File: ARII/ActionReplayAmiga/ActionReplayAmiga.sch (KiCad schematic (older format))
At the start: 33 parts, among them J0 A2000_CPUSLOT_EDGE_LOGICAL, Q0 MOSFET_PCH-DMG2307L, SW0 SW_SPST, SW1 SW_SPDT, U0 TIF044 FS F74, U1 16L8-25C (TI036FF), U10 27C512-15_PLCC, U2 16L8-25C (TI036FF), U3 16L8-25C (TI036FF), U4 16L8-25C (TI042FF)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

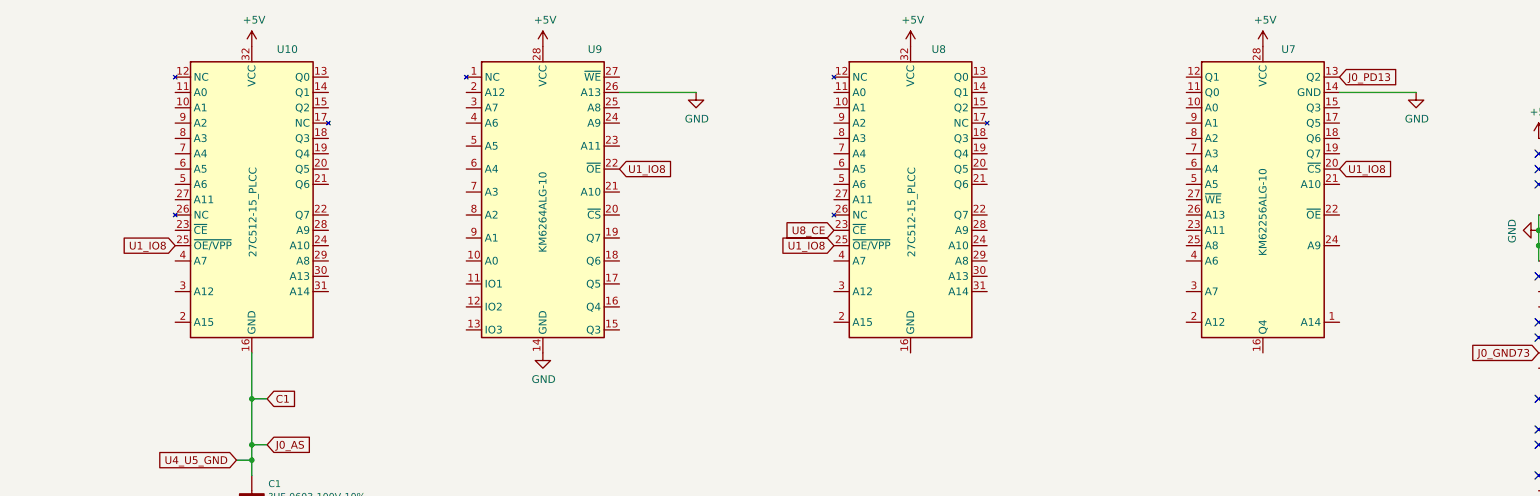
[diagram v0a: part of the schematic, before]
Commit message: Fixed Layouts of KM62256ALG and 27C512-15
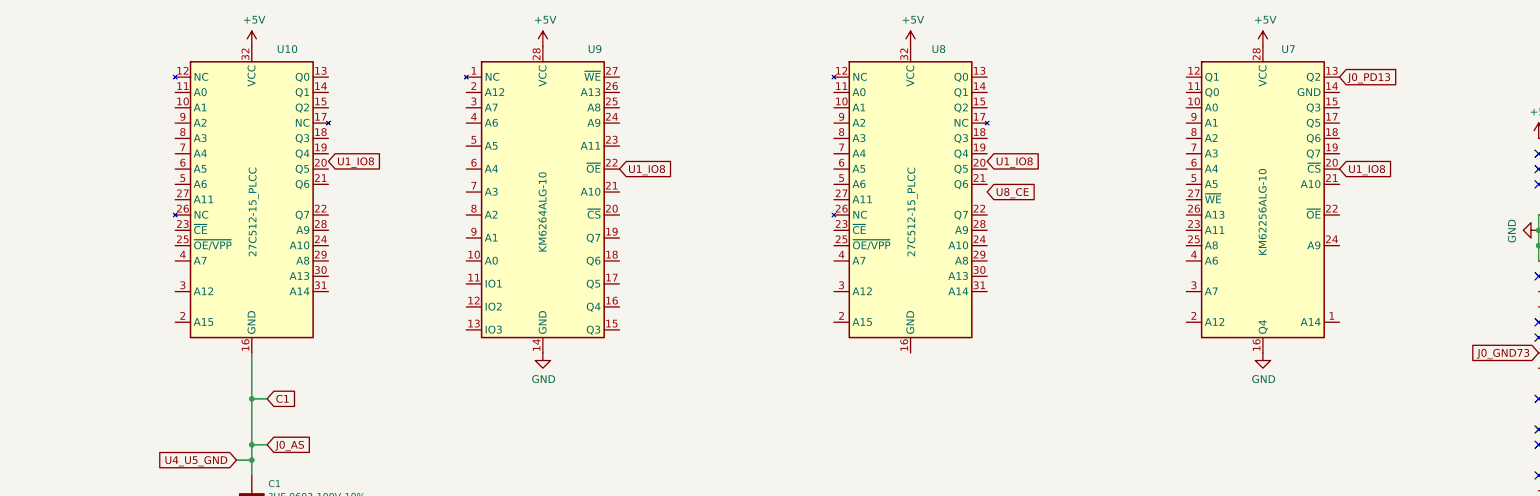
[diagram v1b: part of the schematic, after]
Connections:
- net GND: now also U7.16 (Q4); no longer U7.14 (GND), U9.26 (A13)
- net U1_IO8: no longer U10.25 (~OE/VPP), U8.25 (~OE/VPP)
- net U8_CE: no longer U8.23 (~CE)
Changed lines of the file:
@@
 Wire Notes Line
 	7050 7400 7050 6650
-Text GLabel 4150 2350 0    50   Input ~ 0
+Text GLabel 5150 1800 2    50   Input ~ 0
 U1_IO8
 Text GLabel 3600 4950 2    50   Input ~ 0
@@
 $Comp
 L power:GND #PWR?
-U 1 1 5FF48F3E
-P 7550 1350
-F 0 "#PWR?" H 7550 1100 50  0001 C CNN
-F 1 "GND" H 7555 1177 50  0000 C CNN
-F 2 "" H 7550 1350 50  0001 C CNN
-F 3 "" H 7550 1350 50  0001 C CNN
-	1    7550 1350
-	1    0    0    -1
-$EndComp
-Wire Wire Line
-	7050 1350 7550 1350
-$Comp
-L power:GND #PWR?
 U 1 1 5FB2E5AA
 P 6550 3050
@@
 	1    0    0    -1
 $EndComp
-Text GLabel 8450 2350 0    50   Input ~ 0
+Text GLabel 9450 1800 2    50   Input ~ 0
 U1_IO8
 $Comp
@@
 	1    0    0    -1
 $EndComp
-Text GLabel 8450 2250 0    50   Input ~ 0
+Text GLabel 9450 2000 2    50   Input ~ 0
 U8_CE
 $Comp
@@
 L power:GND #PWR?
 U 1 1 5FB2FA5B
-P 12250 1350
-F 0 "#PWR?" H 12250 1100 50  0001 C CNN
-F 1 "GND" H 12255 1177 50  0000 C CNN
-F 2 "" H 12250 1350 50  0001 C CNN
-F 3 "" H 12250 1350 50  0001 C CNN
-	1    12250 1350
-	1    0    0    -1
-$EndComp
-Text GLabel 11750 1250 2    50   Input ~ 0
-J0_PD13
-Wire Wire Line
-	11750 1350 12250 1350
+P 11250 3050
+F 0 "#PWR?" H 11250 2800 50  0001 C CNN
+F 1 "GND" H 11255 2877 50  0000 C CNN
+F 2 "" H 11250 3050 50  0001 C CNN
+F 3 "" H 11250 3050 50  0001 C CNN
+	1    11250 3050
+	1    0    0    -1
+$EndComp
 $Comp
 L power:+5V #PWR?
@@
 	1    0    0    -1
 $EndComp
-Text GLabel 11750 1850 2    50   Input ~ 0
-U1_IO8
 $Comp
 L ActionReplayAmiga:KM6264ALG-10 U9
@@
 	1    0    0    -1
 $EndComp
+Text GLabel 11750 1850 2    50   Input ~ 0
+U1_IO8
+Text GLabel 11750 1250 2    50   Input ~ 0
+J0_PD13
 $EndSCHEMATC

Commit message: U2 Completed
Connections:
- net U2_I1: now reaches U2.1 (I1)
- net U2_I1: now also U3.1 (I1)
- net U9_CS1: now reaches U2.16 (IO4)
- net U9_CS1: now also U9.20 (~CS)
- net U9_IO1: now reaches U2.17 (I03)
- net U9_IO1: now also U9.11 (IO1)
- net U9_IO2: now reaches U2.18 (IO2)
- net U9_IO2: now also U9.12 (IO2)
- net U7_CS: now reaches U2.19 (IO1)
- net U7_CS: now also U7.22 (~OE)
- net U2_I2: now reaches U2.2 (I2)
- net U2_I2: now also U3.2 (I2)
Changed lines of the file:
@@
 Text GLabel 11750 1250 2    50   Input ~ 0
 J0_PD13
+Text GLabel 7050 2150 2    50   Input ~ 0
+U9_CS1
+Text GLabel 6200 4650 2    50   Input ~ 0
+U9_CS1
+Text GLabel 6050 2600 0    50   Input ~ 0
+U9_IO1
+Text GLabel 6200 4550 2    50   Input ~ 0
+U9_IO1
+Text GLabel 6050 2750 0    50   Input ~ 0
+U9_IO2
+Text GLabel 6200 4450 2    50   Input ~ 0
+U9_IO2
+Text GLabel 11750 2150 2    50   Input ~ 0
+U7_CS
+Text GLabel 6200 4350 2    50   Input ~ 0
+U7_CS
+Text GLabel 5200 4450 0    50   Input ~ 0
+U2_I2
+Text GLabel 6950 4400 0    50   Input ~ 0
+U2_I2
+Text GLabel 5200 4350 0    50   Input ~ 0
+U2_I1
+Text GLabel 6950 4300 0    50   Input ~ 0
+U2_I1
 $EndSCHEMATC

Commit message: U3 Completed
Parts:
- removed SW0: SW_SPST, symbol Switch:SW_SPST
- added S0: GPTS203211B, digikey-footprints:PushButton_12x12mm_THT_GPTS203211B, symbol dk_Pushbutton-Switches:GPTS203211B
- gave numbers to parts that had none: 1
- renumbered SW1 to SW0
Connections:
- net labels added: J0_A9, U2_IO8, U3_I6, U3_I8, U3_I9
- wire segments 107 -> 117
- no-connect marks 32 -> 35
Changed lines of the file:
@@
 NoConn ~ 13050 2950
 $Comp
-L power:GND #PWR?
+L power:GND #PWR0101
 U 1 1 5FB0800F
 P 10700 9200
-F 0 "#PWR?" H 10700 8950 50  0001 C CNN
+F 0 "#PWR0101" H 10700 8950 50  0001 C CNN
 F 1 "GND" H 10705 9027 50  0000 C CNN
 F 2 "" H 10700 9200 50  0001 C CNN
@@
 $EndComp
 $Comp
-L power:+5V #PWR?
+L power:+5V #PWR0102
 U 1 1 5FB0A7A1
 P 13050 1650
-F 0 "#PWR?" H 13050 1500 50  0001 C CNN
+F 0 "#PWR0102" H 13050 1500 50  0001 C CNN
 F 1 "+5V" H 13065 1823 50  0000 C CNN
 F 2 "" H 13050 1650 50  0001 C CNN
@@
 	10700 9050 10700 9200
 $Comp
-L power:GND #PWR?
+L power:GND #PWR0103
 U 1 1 5FB0CDC8
 P 13050 2250
-F 0 "#PWR?" H 13050 2000 50  0001 C CNN
+F 0 "#PWR0103" H 13050 2000 50  0001 C CNN
 F 1 "GND" H 13055 2077 50  0000 C CNN
 F 2 "" H 13050 2250 50  0001 C CNN
@@
 	10700 9200 10700 9400
 $Comp
-L power:+5V #PWR?
+L power:+5V #PWR0104
 U 1 1 5FB10955
 P 10700 8750
-F 0 "#PWR?" H 10700 8600 50  0001 C CNN
+F 0 "#PWR0104" H 10700 8600 50  0001 C CNN
 F 1 "+5V" H 10715 8923 50  0000 C CNN
 F 2 "" H 10700 8750 50  0001 C CNN
@@
 U1_I8
 $Comp
-L power:GND #PWR?
+L power:GND #PWR0105
 U 1 1 5FB26A46
 P 6750 5450
-F 0 "#PWR?" H 6750 5200 50  0001 C CNN
+F 0 "#PWR0105" H 6750 5200 50  0001 C CNN
 F 1 "GND" H 6755 5277 50  0000 C CNN
 F 2 "" H 6750 5450 50  0001 C CNN
@@
 $EndComp
 $Comp
-L power:GND #PWR?
+L power:GND #PWR0106
 U 1 1 5FB276CF
 P 2300 8200
-F 0 "#PWR?" H 2300 7950 50  0001 C CNN
+F 0 "#PWR0106" H 2300 7950 50  0001 C CNN
 F 1 "GND" H 2305 8027 50  0000 C CNN
 F 2 "" H 2300 8200 50  0001 C CNN
@@
 $EndComp
 $Comp
-L power:+5V #PWR?
+L power:+5V #PWR0107
 U 1 1 5FEE02E0
 P 2900 7100
-F 0 "#PWR?" H 2900 6950 50  0001 C CNN
+F 0 "#PWR0107" H 2900 6950 50  0001 C CNN
 F 1 "+5V" H 2915 7273 50  0000 C CNN
 F 2 "" H 2900 7100 50  0001 C CNN
@@
 $EndComp
 $Comp
-L Amiga-Conn:A2000_CPUSLOT_EDGE_PHYS J?
+L Amiga-Conn:A2000_CPUSLOT_EDGE_PHYS J1
 U 1 1 5FEEBC0A
 P 15700 5550
-F 0 "J?" V 11353 5487 60  0000 C CNN
+F 0 "J1" V 11353 5487 60  0000 C CNN
 F 1 "A2000_CPUSLOT_EDGE_PHYS" V 11459 5487 60  0000 C CNN
 F 2 "" H 13000 7000 60  0001 C CNN
@@
 $EndComp
 $Comp
-L power:+5V #PWR?
+L power:+5V #PWR0108
 U 1 1 5FF201E6
 P 1150 7400
-F 0 "#PWR?" H 1150 7250 50  0001 C CNN
+F 0 "#PWR0108" H 1150 7250 50  0001 C CNN
 F 1 "+5V" H 1165 7573 50  0000 C CNN
 F 2 "" H 1150 7400 50  0001 C CNN
@@
 U0_12PRE
 $Comp
-L power:GND #PWR?
+L power:GND #PWR0109
 U 1 1 5FF21609
 P 1150 7500
-F 0 "#PWR?" H 1150 7250 50  0001 C CNN
+F 0 "#PWR0109" H 1150 7250 50  0001 C CNN
 F 1 "GND" H 1155 7327 50  0000 C CNN
 F 2 "" H 1150 7500 50  0001 C CNN
@@
 	1800 7800 1300 7800
 $Comp
-L power:+5V #PWR?
+L power:+5V #PWR0110
 U 1 1 5FF51C54
 P 1300 7800
-F 0 "#PWR?" H 1300 7650 50  0001 C CNN
+F 0 "#PWR0110" H 1300 7650 50  0001 C CNN
 F 1 "+5V" H 1315 7973 50  0000 C CNN
 F 2 "" H 1300 7800 50  0001 C CNN
@@
 	3500 8700 3500 9000
 $Comp
-L power:GND #PWR?
+L power:GND #PWR0111
 U 1 1 5FF30BC6
 P 3500 9550
-F 0 "#PWR?" H 3500 9300 50  0001 C CNN
+F 0 "#PWR0111" H 3500 9300 50  0001 C CNN
 F 1 "GND" H 3505 9377 50  0000 C CNN
 F 2 "" H 3500 9550 50  0001 C CNN
@@
 	6200 9600 6750 9600
 $Comp
-L power:GND #PWR?
+L power:GND #PWR0112
 U 1 1 5FF35B64
 P 6750 9600
-F 0 "#PWR?" H 6750 9350 50  0001 C CNN
+F 0 "#PWR0112" H 6750 9350 50  0001 C CNN
 F 1 "GND" H 6755 9427 50  0000 C CNN
 F 2 "" H 6750 9600 50  0001 C CNN
@@
 $EndComp
 $Comp
-L power:GND #PWR?
+L power:GND #PWR0113
 U 1 1 5FF39A19
 P 3950 9600
-F 0 "#PWR?" H 3950 9350 50  0001 C CNN
+F 0 "#PWR0113" H 3950 9350 50  0001 C CNN
 F 1 "GND" H 3955 9427 50  0000 C CNN
 F 2 "" H 3950 9600 50  0001 C CNN
@@
 Connection ~ 5400 9000
 $Comp
-L power:+5V #PWR?
+L power:+5V #PWR0114
 U 1 1 5FF5A056
 P 6450 8850
-F 0 "#PWR?" H 6450 8700 50  0001 C CNN
+F 0 "#PWR0114" H 6450 8700 50  0001 C CNN
 F 1 "+5V" H 6465 9023 50  0000 C CNN
 F 2 "" H 6450 8850 50  0001 C CNN
@@
 U1_I5
 $Comp
-L power:GND #PWR?
+L power:GND #PWR0115
 U 1 1 5FFA6750
 P 5450 7800
-F 0 "#PWR?" H 5450 7550 50  0001 C CNN
+F 0 "#PWR0115" H 5450 7550 50  0001 C CNN
 F 1 "GND" H 5455 7627 50  0000 C CNN
 F 2 "" H 5450 7800 50  0001 C CNN
@@
 	2500 7600 2750 7600
 $Comp
-L Switch:SW_SPDT SW1
+L Switch:SW_SPDT SW0
 U 1 1 6006069C
 P 8300 8550
-F 0 "SW1" H 8300 8225 50  0000 C CNN
+F 0 "SW0" H 8300 8225 50  0000 C CNN
 F 1 "SW_SPDT" H 8300 8316 50  0000 C CNN
 F 2 "" H 8300 8550 50  0001 C CNN
@@
 Wire Wire Line
 	5150 7800 5150 7950
-$Comp
-L Switch:SW_SPST SW0
-U 1 1 60077917
-P 4850 7950
-F 0 "SW0" H 4850 8185 50  0000 C CNN
-F 1 "SW_SPST" H 4850 8094 50  0000 C CNN
-F 2 "" H 4850 7950 50  0001 C CNN
-F 3 "~" H 4850 7950 50  0001 C CNN
-	1    4850 7950
-	1    0    0    -1
-$EndComp
 Wire Wire Line
 	5050 7950 5150 7950
@@
 	5150 7950 5150 8300
 Wire Wire Line
-	4450 7950 4650 7950
-$Comp
-L power:+5V #PWR?
+	4450 7950 4550 7950
+$Comp
+L power:+5V #PWR0116
 U 1 1 600D8BB7
 P 7750 8750
-F 0 "#PWR?" H 7750 8600 50  0001 C CNN
+F 0 "#PWR0116" H 7750 8600 50  0001 C CNN
 F 1 "+5V" H 7765 8923 50  0000 C CNN
 F 2 "" H 7750 8750 50  0001 C CNN
@@
 $EndComp
 $Comp
-L power:+5V #PWR?
+L power:+5V #PWR0117
 U 1 1 600E1C71
 P 8700 7400
-F 0 "#PWR?" H 8700 7250 50  0001 C CNN
+F 0 "#PWR0117" H 8700 7250 50  0001 C CNN
 F 1 "+5V" H 8715 7573 50  0000 C CNN
 F 2 "" H 8700 7400 50  0001 C CNN
@@
 Wire Notes Line
 	7050 7400 7050 6650
-Text GLabel 5150 1800 2    50   Input ~ 0
+Text GLabel 5350 1800 2    50   Input ~ 0
 U1_IO8
 Text GLabel 3600 4950 2    50   Input ~ 0
@@
 	9400 5400 11350 5400
 $Comp
-L power:+5V #PWR?
+L power:+5V #PWR0118
 U 1 1 5FF40B6C
 P 4650 1050
-F 0 "#PWR?" H 4650 900 50  0001 C CNN
+F 0 "#PWR0118" H 4650 900 50  0001 C CNN
 F 1 "+5V" H 4665 1223 50  0000 C CNN
 F 2 "" H 4650 1050 50  0001 C CNN
@@
 Text GLabel 6200 4750 2    50   Input ~ 0
 U8_CE
-Text GLabel 7050 1850 2    50   Input ~ 0
-U1_IO8
-$Comp
-L power:+5V #PWR?
+$Comp
+L power:+5V #PWR0119
 U 1 1 5FF44F56
 P 6550 1050
-F 0 "#PWR?" H 6550 900 50  0001 C CNN
+F 0 "#PWR0119" H 6550 900 50  0001 C CNN
 F 1 "+5V" H 6565 1223 50  0000 C CNN
 F 2 "" H 6550 1050 50  0001 C CNN
@@
 $EndComp
 $Comp
-L power:GND #PWR?
+L power:GND #PWR0120
 U 1 1 5FB2E5AA
 P 6550 3050
-F 0 "#PWR?" H 6550 2800 50  0001 C CNN
+F 0 "#PWR0120" H 6550 2800 50  0001 C CNN
 F 1 "GND" H 6555 2877 50  0000 C CNN
 F 2 "" H 6550 3050 50  0001 C CNN
@@
 	1    0    0    -1
 $EndComp
-Text GLabel 9450 1800 2    50   Input ~ 0
+Text GLabel 9800 1800 2    50   Input ~ 0
 U1_IO8
 $Comp
-L power:+5V #PWR?
+L power:+5V #PWR0121
 U 1 1 5FF4196F
 P 8950 1050
-F 0 "#PWR?" H 8950 900 50  0001 C CNN
+F 0 "#PWR0121" H 8950 900 50  0001 C CNN
 F 1 "+5V" H 8965 1223 50  0000 C CNN
 F 2 "" H 8950 1050 50  0001 C CNN
@@
 $EndComp
 $Comp
-L power:GND #PWR?
+L power:GND #PWR0122
 U 1 1 5FB2FA5B
 P 11250 3050
-F 0 "#PWR?" H 11250 2800 50  0001 C CNN
+F 0 "#PWR0122" H 11250 2800 50  0001 C CNN
 F 1 "GND" H 11255 2877 50  0000 C CNN
 F 2 "" H 11250 3050 50  0001 C CNN
@@
 $EndComp
 $Comp
-L power:+5V #PWR?
+L power:+5V #PWR0123
 U 1 1 602844FA
 P 11250 1050
-F 0 "#PWR?" H 11250 900 50  0001 C CNN
+F 0 "#PWR0123" H 11250 900 50  0001 C CNN
 F 1 "+5V" H 11265 1223 50  0000 C CNN
 F 2 "" H 11250 1050 50  0001 C CNN
@@
 	1    0    0    -1
 $EndComp
-Text GLabel 11750 1850 2    50   Input ~ 0
-U1_IO8
 Text GLabel 11750 1250 2    50   Input ~ 0
 J0_PD13
@@
 Text GLabel 6950 4300 0    50   Input ~ 0
 U2_I1
+$Comp
+L dk_Pushbutton-Switches:GPTS203211B S0
+U 1 1 5FEFCEF5
+P 4850 7950
+F 0 "S0" H 4850 8225 50  0000 C CNN
+F 1 "GPTS203211B" H 4850 8134 50  0000 C CNN
+F 2 "digikey-footprints:PushButton_12x12mm_THT_GPTS203211B" H 5050 8150 50  0001 L CNN
+F 3 "http://switches-connectors-custom.cwind.com/Asset/GPTS203211BR2.pdf" H 5050 8250 60  0001 L CNN
+F 4 "CW181-ND" H 5050 8350 60  0001 L CNN "Digi-Key_PN"
+F 5 "GPTS203211B" H 5050 8450 60  0001 L CNN "MPN"
+F 6 "Switches" H 5050 8550 60  0001 L CNN "Category"
+F 7 "Pushbutton Switches" H 5050 8650 60  0001 L CNN "Family"
+F 8 "http://switches-connectors-custom.cwind.com/Asset/GPTS203211BR2.pdf" H 5050 8750 60  0001 L CNN "DK_Datasheet_Link"
+F 9 "/product-detail/en/cw-industries/GPTS203211B/CW181-ND/3190590" H 5050 8850 60  0001 L CNN "DK_Detail_Page"
+F 10 "SWITCH PUSHBUTTON SPST 1A 30V" H 5050 8950 60  0001 L CNN "Description"
+F 11 "CW Industries" H 5050 9050 60  0001 L CNN "Manufacturer"
+F 12 "Active" H 5050 9150 60  0001 L CNN "Status"
+	1    4850 7950
+	1    0    0    -1
+$EndComp
+Text GLabel 5150 2000 2    50   Input ~ 0
+U2_IO8
+Text GLabel 6200 5050 2    50   Input ~ 0
+U2_IO8
+Text GLabel 6950 4800 0    50   Input ~ 0
+U3_I6
+Text GLabel 4550 8000 3    50   Input ~ 0
+U3_I6
+Wire Wire Line
+	4550 8000 4550 7950
+Connection ~ 4550 7950
+Wire Wire Line
+	4550 7950 4650 7950
+Text GLabel 14750 2450 2    50   Input ~ 0
+J0_A9
+Text GLabel 6950 4900 0    50   Input ~ 0
+J0_A9
+Text GLabel 6950 5000 0    50   Input ~ 0
+U3_I8
+Text GLabel 9900 4800 2    50   Input ~ 0
+U3_I8
+Text GLabel 5350 1700 2    50   Input ~ 0
+U3_I9
+Text GLabel 6950 5100 0    50   Input ~ 0
+U3_I9
+Text GLabel 9800 1700 2    50   Input ~ 0
+U3_I9
+Wire Wire Line
+	9450 1800 9800 1800
+Wire Wire Line
+	9800 1800 9800 1700
+Wire Wire Line
+	5150 1800 5350 1800
+Wire Wire Line
+	5350 1800 5350 1700
+Text GLabel 7250 1850 2    50   Input ~ 0
+U1_IO8
+Text GLabel 7250 1750 2    50   Input ~ 0
+U3_I9
+Wire Wire Line
+	7050 1850 7250 1850
+Wire Wire Line
+	7250 1850 7250 1750
+Text GLabel 12100 1850 2    50   Input ~ 0
+U1_IO8
+Text GLabel 12100 1750 2    50   Input ~ 0
+U3_I9
+Wire Wire Line
+	11750 1850 12100 1850
+Wire Wire Line
+	12100 1850 12100 1750
+NoConn ~ 7950 5000
+NoConn ~ 7950 4900
+NoConn ~ 7950 4300
 $EndSCHEMATC
